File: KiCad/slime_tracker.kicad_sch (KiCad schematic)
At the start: 51 parts, among them J1 batt, J2 Extension, J3 USB_C_Receptacle_PowerOnly_6P, SW1 SW_DPDT_x2, U1 TP4056, U3 TPS7A0333PDBVR, U4 ESP32 SUPER MINI C3, U5 TPS61090

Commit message: Rev_02
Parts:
- removed R12: 10kΩ, Resistor_SMD:R_0603_1608Metric, symbol Device:R
- R11: value 2kΩ -> 3kΩ
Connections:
- net AGND: now also U1.9 (EP_GND), U5.17 (EP_GND)
- net at C13.1, D1.2 (A), D2.2 (A)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: no longer U1.1 (TEMP)
- no-connect marks 0 -> 1
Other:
- note removed: "!!!ERROR!!! !!!ERROR!!! !!!ERROR!!! !!!ERROR!!! !!!ERROR!!! !!!ERROR!!! !!!ERROR!!! !!!ERROR!!!"
- moved on the sheet: C12, C13, D1, D2, J3, R11, R13, R14, R15, R16, R17, R19

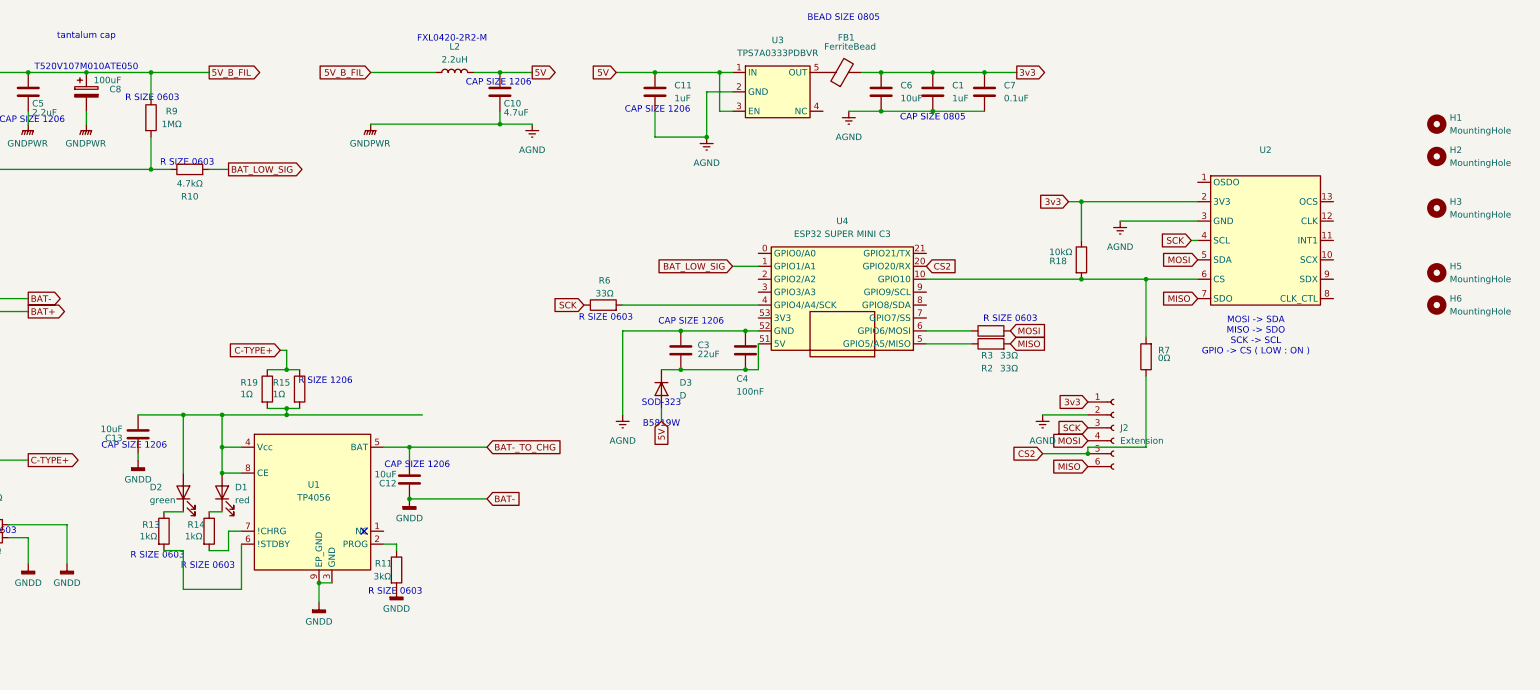
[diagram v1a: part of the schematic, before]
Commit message: IC2, SPI explain added
and N.C R added
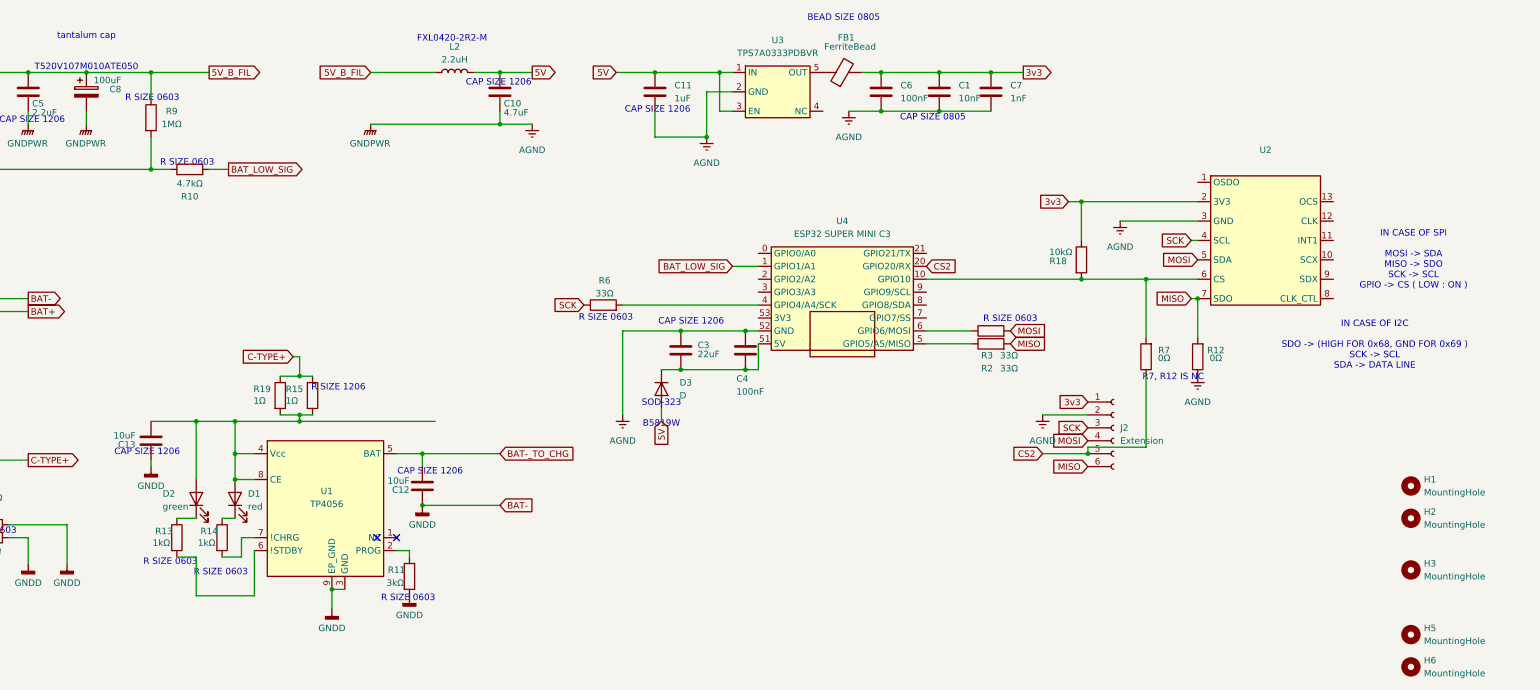
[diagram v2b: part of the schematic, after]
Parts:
- added R12: 0Ω, Resistor_SMD:R_0603_1608Metric, symbol Device:R
- C1: value 1uF -> 10nF
- C6: value 10uF -> 100nF
- C7: value 0.1uF -> 1nF
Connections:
- net AGND: now also R12.1
- net MISO: now also R12.2
- no-connect marks 1 -> 2
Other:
- note added: "IN CASE OF I2C SDO -> (HIGH FOR 0x68, GND FOR 0x69 ) SCK -> SCL SDA -> DATA LINE"
- note added: "IN CASE OF SPI MOSI -> SDA MISO -> SDO SCK -> SCL GPIO -> CS ( LOW : ON )"
- note added: "R7, R12 IS NC"
- note removed: "MOSI -> SDA MISO -> SDO SCK -> SCL GPIO -> CS ( LOW : ON )"
- moved on the sheet: C1, C12, C13, C7, D1, D2, H1, H2, H3, H5, H6, R11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
